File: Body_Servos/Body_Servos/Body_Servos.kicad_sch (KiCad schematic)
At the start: 30 parts, among them J1 USB_B_Micro, J12 SERIAL_FU, J2 AUX3, J3 AUX1, J4 AUX2, J5 12OUT, J6 12VOUT, J7 5V OUT, J8 5V Out 2, SW1 SW_Push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

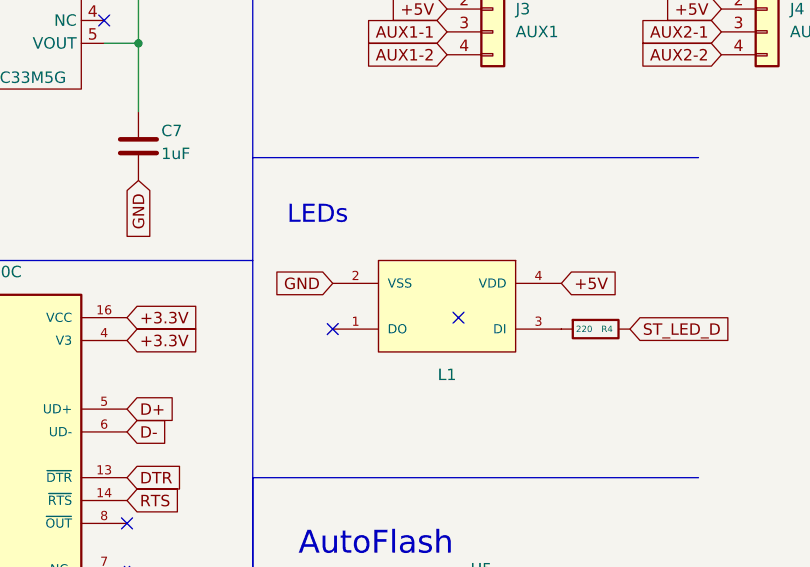
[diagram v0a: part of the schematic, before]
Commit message: added LED PCBs
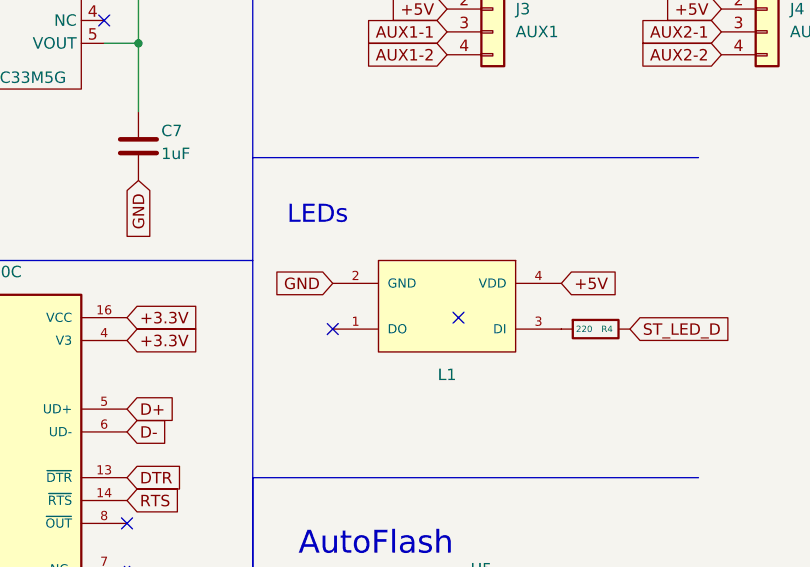
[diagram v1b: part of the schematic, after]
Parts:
- J2, J3, J4: LCSC (none) -> C240840
- L1: footprint Custom:WS2812B-2020 -> WS2812B-2020
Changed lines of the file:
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@@
       (effects (font (size 1.27 1.27)) hide)
     )
-    (property "Datasheet" "~" (id 3) (at 154.94 158.75 0)
+    (property "Datasheet" "https://datasheet.lcsc.com/lcsc/2001160007_Cixi-Kefa-Elec-KF350-3-5-2P_C474892.pdf" (id 3) (at 154.94 158.75 0)
       (effects (font (size 1.27 1.27)) hide)
     )
@@
       (effects (font (size 1.27 1.27)) hide)
     )
-    (property "Datasheet" "" (id 3) (at 181.61 55.88 0)
+    (property "Datasheet" "https://datasheet.lcsc.com/lcsc/1811131510_MICRONE-Nanjing-Micro-One-Elec-ME6211C33M5G-N_C82942.pdf" (id 3) (at 181.61 55.88 0)
       (effects (font (size 1.27 1.27)) hide)
     )
@@
       (effects (font (size 1.27 1.27)) hide)
     )
-    (property "Datasheet" "" (id 3) (at 74.93 53.34 0)
+    (property "Datasheet" "https://datasheet.lcsc.com/lcsc/2005211207_Espressif-Systems-ESP32-WROOM-32D-N16_C529578.pdf" (id 3) (at 74.93 53.34 0)
       (effects (font (size 1.27 1.27)) hide)
     )
@@
       (effects (font (size 1.27 1.27)) hide)
     )
-    (property "Datasheet" "~" (id 3) (at 154.94 134.62 0)
+    (property "Datasheet" "https://datasheet.lcsc.com/lcsc/2001160007_Cixi-Kefa-Elec-KF350-3-5-2P_C474892.pdf" (id 3) (at 154.94 134.62 0)
       (effects (font (size 1.27 1.27)) hide)
     )
@@
       (effects (font (size 1.27 1.27)) hide)
     )
-    (property "Datasheet" "" (id 3) (at 139.7 41.91 0)
+    (property "Datasheet" "https://datasheet.lcsc.com/lcsc/1809141711_Jiangsu-Changjing-Electronics-Technology-Co---Ltd--CJ2301-S1_C8547.pdf" (id 3) (at 139.7 41.91 0)
       (effects (font (size 1.27 1.27)) hide)
     )
@@
       (effects (font (size 1.27 1.27)) hide)
     )
-    (property "Datasheet" "~" (id 3) (at 132.08 93.98 0)
+    (property "Datasheet" "https://datasheet.lcsc.com/lcsc/1811131822_Amphenol-ICC-10118194-0001LF_C132563.pdf" (id 3) (at 132.08 93.98 0)
       (effects (font (size 1.27 1.27)) hide)
     )
@@
       (effects (font (size 1.27 1.27)) hide)
     )
-    (property "Datasheet" "~" (id 3) (at 154.94 143.51 0)
+    (property "Datasheet" "https://datasheet.lcsc.com/lcsc/2001160007_Cixi-Kefa-Elec-KF350-3-5-2P_C474892.pdf" (id 3) (at 154.94 143.51 0)
       (effects (font (size 1.27 1.27)) hide)
     )
@@
       (effects (font (size 1.27 1.27)) hide)
     )
-    (property "Datasheet" "~" (id 3) (at 154.94 57.15 0)
+    (property "Datasheet" "https://datasheet.lcsc.com/lcsc/1811081616_Murata-Electronics-GRM155R61E105KA12D_C77009.pdf" (id 3) (at 154.94 57.15 0)
       (effects (font (size 1.27 1.27)) hide)
     )
@@
       (effects (font (size 1.27 1.27)) hide)
     )
-    (property "Datasheet" "~" (id 3) (at 40.64 86.36 0)
+    (property "Datasheet" "https://datasheet.lcsc.com/lcsc/1810191222_Samsung-Electro-Mechanics-CL05B104KB54PNC_C307331.pdf" (id 3) (at 40.64 86.36 0)
       (effects (font (size 1.27 1.27)) hide)
     )
@@
       (effects (font (size 1.27 1.27)) (justify left bottom) hide)
     )
-    (property "Footprint" "Custom:WS2812B-2020" (id 2) (at 232.41 74.93 0)
-      (effects (font (size 1.27 1.27)) (justify left bottom) hide)
-    )
-    (property "Datasheet" "" (id 3) (at 232.41 74.93 0)
+    (property "Footprint" "WS2812B-2020" (id 2) (at 232.41 74.93 0)
+      (effects (font (size 1.27 1.27)) (justify left bottom) hide)
+    )
+    (property "Datasheet" "https://datasheet.lcsc.com/lcsc/2012110135_Worldsemi-WS2812B-2020_C965555.pdf" (id 3) (at 232.41 74.93 0)
       (effects (font (size 1.27 1.27)) (justify left bottom) hide)
     )
@@
       (effects (font (size 1.27 1.27)) hide)
     )
-    (property "Datasheet" "~" (id 3) (at 157.48 100.33 0)
+    (property "Datasheet" "https://datasheet.lcsc.com/lcsc/1810191222_Samsung-Electro-Mechanics-CL05B104KB54PNC_C307331.pdf" (id 3) (at 157.48 100.33 0)
       (effects (font (size 1.27 1.27)) hide)
     )
@@
       (effects (font (size 1.27 1.27)) hide)
     )
-    (property "Datasheet" "~" (id 3) (at 267.97 41.91 0)
+    (property "Datasheet" "https://datasheet.lcsc.com/lcsc/1811051309_MOLEX-470531000_C240840.pdf" (id 3) (at 267.97 41.91 0)
+      (effects (font (size 1.27 1.27)) hide)
+    )
+    (property "LCSC" "C240840 " (id 4) (at 267.97 41.91 0)
       (effects (font (size 1.27 1.27)) hide)
     )
@@
       (effects (font (size 1.27 1.27)) hide)
     )
-    (property "Datasheet" "~" (id 3) (at 198.12 57.15 0)
+    (property "Datasheet" "https://datasheet.lcsc.com/lcsc/1811081616_Murata-Electronics-GRM155R61E105KA12D_C77009.pdf" (id 3) (at 198.12 57.15 0)
       (effects (font (size 1.27 1.27)) hide)
     )
@@
       (effects (font (size 1.27 1.27)) (justify left bottom) hide)
     )
-    (property "Datasheet" "" (id 3) (at 234.95 111.76 0)
+    (property "Datasheet" "https://datasheet.lcsc.com/lcsc/1809211024_Jiangsu-Changjing-Electronics-Technology-Co---Ltd--UMH3N_C62892.pdf" (id 3) (at 234.95 111.76 0)
       (effects (font (size 1.27 1.27)) (justify left bottom) hide)
     )
@@
       (effects (font (size 1.27 1.27)) hide)
     )
-    (property "Datasheet" "~" (id 3) (at 143.51 57.15 0)
+    (property "Datasheet" "https://datasheet.lcsc.com/lcsc/2206010045_UNI-ROYAL-Uniroyal-Elec-0603WAF1003T5E_C25803.pdf" (id 3) (at 143.51 57.15 0)
       (effects (font (size 1.27 1.27)) hide)
     )
@@
       (effects (font (size 1.27 1.27)) hide)
     )
-    (property "Datasheet" "~" (id 3) (at 267.97 27.94 0)
+    (property "Datasheet" "https://datasheet.lcsc.com/lcsc/1912230932_MOLEX-22272031_C471416.pdf" (id 3) (at 267.97 27.94 0)
       (effects (font (size 1.27 1.27)) hide)
     )
@@
       (effects (font (size 1.27 1.27)) hide)
     )
-    (property "Datasheet" "~" (id 3) (at 154.94 166.37 0)
+    (property "Datasheet" "https://datasheet.lcsc.com/lcsc/2001160007_Cixi-Kefa-Elec-KF350-3-5-2P_C474892.pdf" (id 3) (at 154.94 166.37 0)
       (effects (font (size 1.27 1.27)) hide)
     )
@@
       (effects (font (size 1.27 1.27)) hide)
     )
-    (property "Datasheet" "~" (id 3) (at 33.02 50.8 0)
+    (property "Datasheet" "https://datasheet.lcsc.com/lcsc/2110111130_XKB-Connectivity-TS-1101S-B-B-B-W-A_C692465.pdf" (id 3) (at 33.02 50.8 0)
       (effects (font (size 1.27 1.27)) hide)
     )
@@
       (effects (font (size 1.27 1.27)) hide)
     )
-    (property "Datasheet" "~" (id 3) (at 237.49 41.91 0)
+    (property "Datasheet" "https://datasheet.lcsc.com/lcsc/1811051309_MOLEX-470531000_C240840.pdf" (id 3) (at 237.49 41.91 0)
+      (effects (font (size 1.27 1.27)) hide)
+    )
+    (property "LCSC" "C240840 " (id 4) (at 237.49 41.91 0)
       (effects (font (size 1.27 1.27)) hide)
     )
@@
       (effects (font (size 1.27 1.27)) hide)
     )
-    (property "Datasheet" "~" (id 3) (at 31.75 86.36 0)
+    (property "Datasheet" "https://datasheet.lcsc.com/lcsc/2007131004_Samsung-Electro-Mechanics-CL05A106MP5NUNC_C315248.pdf" (id 3) (at 31.75 86.36 0)
       (effects (font (size 1.27 1.27)) hide)
     )
@@
       (effects (font (size 1.27 1.27)) hide)
     )
-    (property "Datasheet" "~" (id 3) (at 26.67 52.07 0)
+    (property "Datasheet" "https://datasheet.lcsc.com/lcsc/1810191222_Samsung-Electro-Mechanics-CL05B104KB54PNC_C307331.pdf" (id 3) (at 26.67 52.07 0)
       (effects (font (size 1.27 1.27)) hide)
     )
@@
       (effects (font (size 1.27 1.27)) hide)
     )
-    (property "Datasheet" "~" (id 3) (at 237.49 26.67 0)
+    (property "Datasheet" "~https://datasheet.lcsc.com/lcsc/1811051309_MOLEX-470531000_C240840.pdf" (id 3) (at 237.49 26.67 0)
+      (effects (font (size 1.27 1.27)) hide)
+    )
+    (property "LCSC" "C240840 " (id 4) (at 237.49 26.67 0)
       (effects (font (size 1.27 1.27)) hide)
     )
@@
       (effects (font (size 1.27 1.27)) hide)
     )
-    (property "Datasheet" "~" (id 3) (at 38.1 34.29 0)
+    (property "Datasheet" "https://datasheet.lcsc.com/lcsc/1811101830_TyoHM-RMC-0603-10K-F-N_C269701.pdf" (id 3) (at 38.1 34.29 0)
       (effects (font (size 1.27 1.27)) hide)
     )
@@
       (effects (font (size 1.524 1.524)) hide)
     )
-    (property "Datasheet" "" (id 3) (at 144.78 50.8 0)
-      (effects (font (size 1.524 1.524)))
+    (property "Datasheet" "https://datasheet.lcsc.com/lcsc/1810010311_MCC-Micro-Commercial-Components-B5819W-TP_C84354.pdf" (id 3) (at 144.78 50.8 0)
+      (effects (font (size 1.524 1.524)) hide)
     )
     (property "LCSC" "C84354" (id 4) (at 144.78 50.8 0)
@@
       (effects (font (size 1.27 1.27)) hide)
     )
-    (property "Datasheet" "~" (id 3) (at 162.56 48.26 0)
+    (property "Datasheet" "https://datasheet.lcsc.com/lcsc/2206010045_UNI-ROYAL-Uniroyal-Elec-0603WAF1003T5E_C25803.pdf" (id 3) (at 162.56 48.26 0)
       (effects (font (size 1.27 1.27)) hide)
     )
@@
       (effects (font (size 1.27 1.27)) (justify left bottom) hide)
     )
-    (property "Datasheet" "" (id 3) (at 181.61 93.98 0)
+    (property "Datasheet" "https://datasheet.lcsc.com/lcsc/2008191806_WCH-Jiangsu-Qin-Heng-CH340C_C84681.pdf" (id 3) (at 181.61 93.98 0)
       (effects (font (size 1.27 1.27)) (justify left bottom) hide)
     )
@@
       (effects (font (size 1.27 1.27)) hide)
     )
-    (property "Datasheet" "~" (id 3) (at 149.86 100.33 0)
+    (property "Datasheet" "https://datasheet.lcsc.com/lcsc/2007131004_Samsung-Electro-Mechanics-CL05A106MP5NUNC_C315248.pdf" (id 3) (at 149.86 100.33 0)
       (effects (font (size 1.27 1.27)) hide)
     )
@@
     )
     (path "/352b947b-2e30-436f-a33b-c4d45389f7e5"
-      (reference "L1") (unit 1) (value "WS2812B-2020") (footprint "Custom:WS2812B-2020")
+      (reference "L1") (unit 1) (value "WS2812B-2020") (footprint "WS2812B-2020")
     )
     (path "/e64c3073-694a-4368-8652-5a6e7a2016cb"
